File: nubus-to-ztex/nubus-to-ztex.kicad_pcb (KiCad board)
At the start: 4 copper layers, 161.6 x 100 mm, 94 parts, among them J1 Conn_02x07_Odd_Even, J2 47219-2001, J3 Conn_01x06_Male, J4 C96ABC, J5 HDMI_A, J6 USB micro-B, J7 Conn_01x03_Male, J8 Conn_01x02, J9 Conn_02x06_Odd_Even, U1 74LVT125, U10 SN65220, U11 TPS2051C, U12 SN74CB3T1G125DBVR, U13 SN74CB3T3125PWR, U14 SN74CB3T3245PWR, U2 74LVT125, U3 74LVT125, U4 SN74CB3T3125PWR, U5 74LVT245BPW,118, U6 74LVT245BPW,118, U7 74LVT245BPW,118, U8 74LVT245BPW,118, U9 TPD12S016PWR

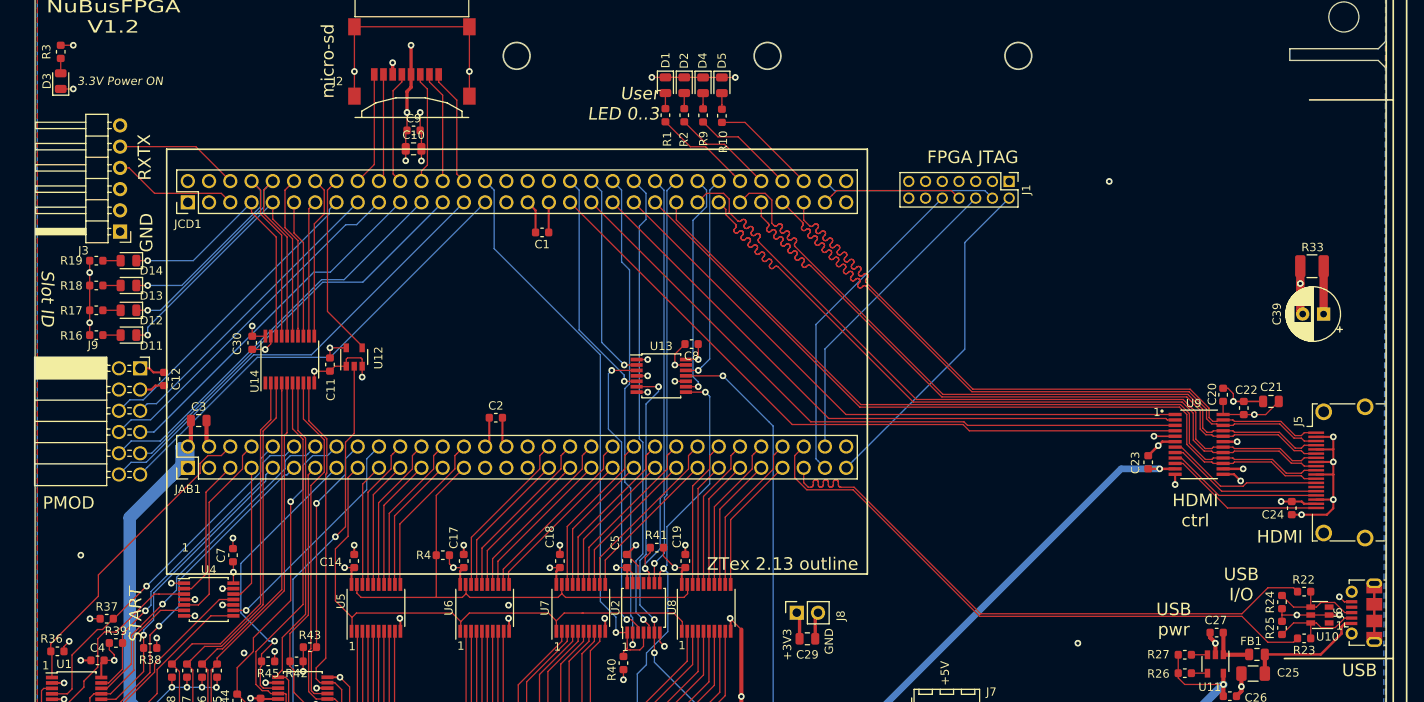
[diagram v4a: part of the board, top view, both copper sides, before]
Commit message: reinstate some useful debug LEDs
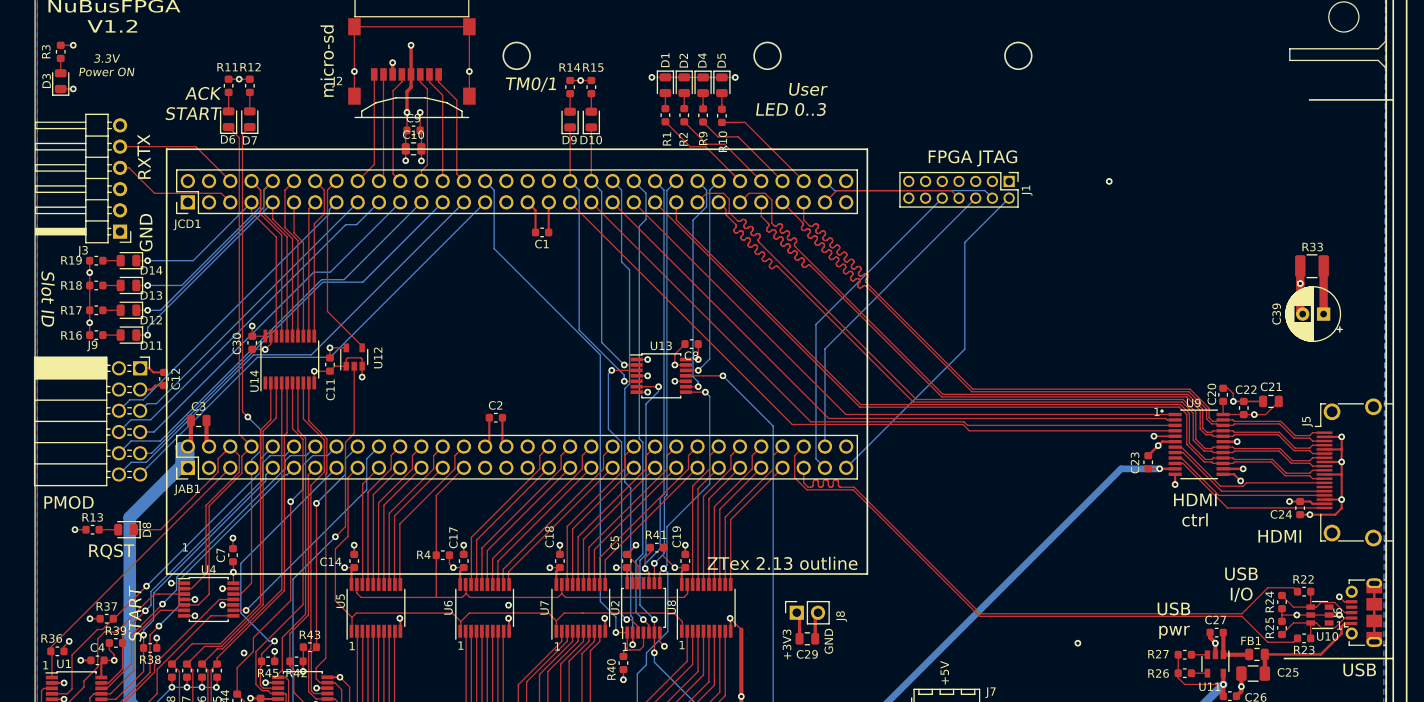
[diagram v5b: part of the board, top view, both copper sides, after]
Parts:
- added D10: YELLOW, LED_SMD:LED_0805_2012Metric, F.Cu at (178.3, 20.1)
- added D6: YELLOW, LED_SMD:LED_0805_2012Metric, F.Cu at (134.9, 20.1)
- added D7: YELLOW, LED_SMD:LED_0805_2012Metric, F.Cu at (137.4, 20.1)
- added D8: YELLOW, LED_SMD:LED_0805_2012Metric, F.Cu at (122.6, 69.2)
- added D9: YELLOW, LED_SMD:LED_0805_2012Metric, F.Cu at (175.7, 20.1)
- added R11: 549, Resistor_SMD:R_0603_1608Metric, F.Cu at (134.9, 16.1)
- added R12: 549, Resistor_SMD:R_0603_1608Metric, F.Cu at (137.4, 16.1)
- added R13: 549, Resistor_SMD:R_0603_1608Metric, F.Cu at (118.6, 69.2)
- added R14: 549, Resistor_SMD:R_0603_1608Metric, F.Cu at (175.7, 16.2)
- added R15: 549, Resistor_SMD:R_0603_1608Metric, F.Cu at (178.3, 16.2)
- moved C24 1.00 mm to (263.0, 66.6)
- moved J5 1.00 mm to (268.9, 62.3)
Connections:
- JAB1 pad 5: ~RQST_3V3 -> ~NMRQ_3V3
- JAB1 pad 6: ~NMRQ_3V3 -> ~RQST_3V3
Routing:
- net ~START_3V3: track 16.5 -> 59.0 mm, vias 0 -> 1
- net ~ACK_3V3: track 23.3 -> 62.6 mm
- net +3V3: track 737.6 -> 771.3 mm, vias 27 -> 30
- net ~RQST_3V3: track 17.3 -> 37.3 mm
- net ~TM1_3V3: track 25.1 -> 31.5 mm
- net ~TM0_3V3: track 28.1 -> 34.5 mm
- net ~NMRQ_3V3: track 37.5 -> 34.0 mm
- net Net-(D7-Pad2): track 0.00 -> 2.28 mm
- net Net-(D8-Pad2): track 0.00 -> 2.28 mm
- net Net-(D6-Pad2): track 0.00 -> 2.28 mm
- net Net-(D9-Pad2): track 0.00 -> 2.16 mm
- net Net-(D10-Pad2): track 0.00 -> 2.16 mm
- net HDMI_D2+: track 83.7 -> 84.7 mm
- net HDMI_D1-: track 87.1 -> 88.1 mm
- net HDMI_D1+: track 88.0 -> 89.0 mm
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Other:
- board text added: "ACK START"
- board text added: "RQST"
- board text added: "TM0/1"

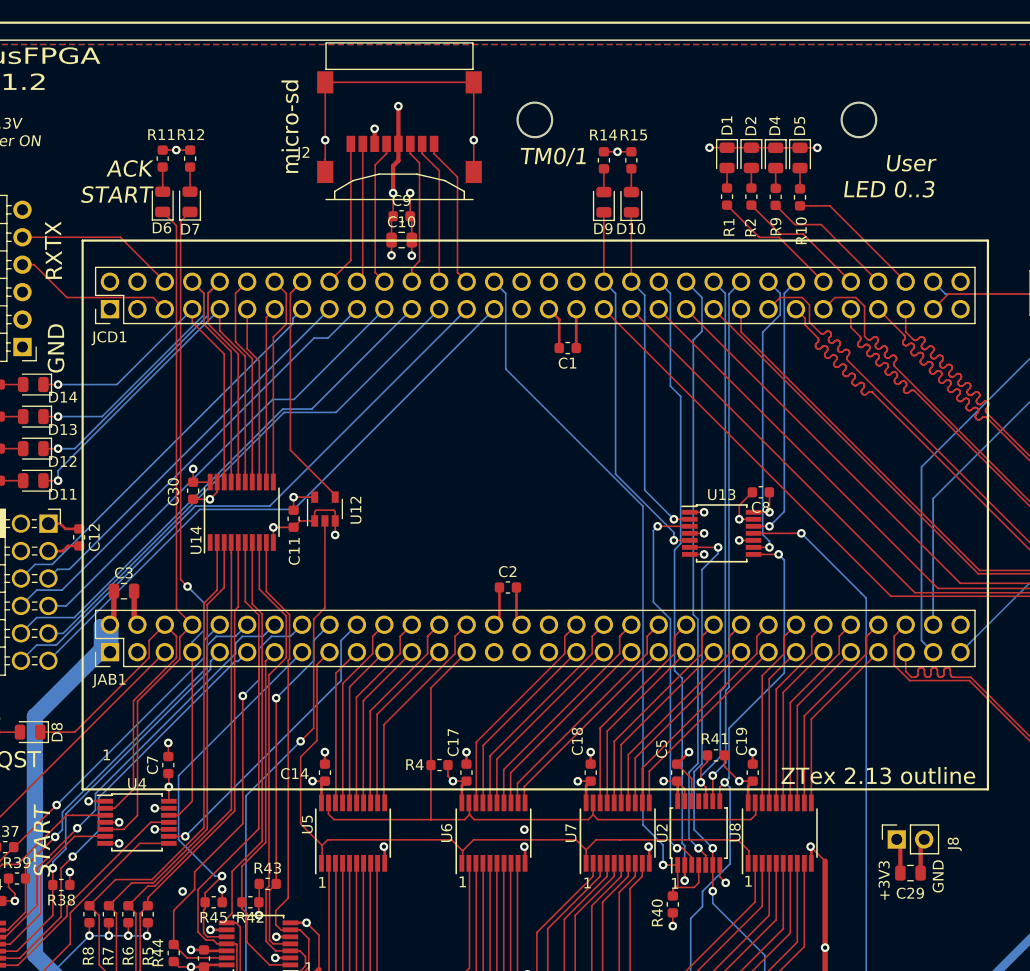
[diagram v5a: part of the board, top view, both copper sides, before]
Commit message: cut down brightness of LEDs, more 2x32 pin headers reference
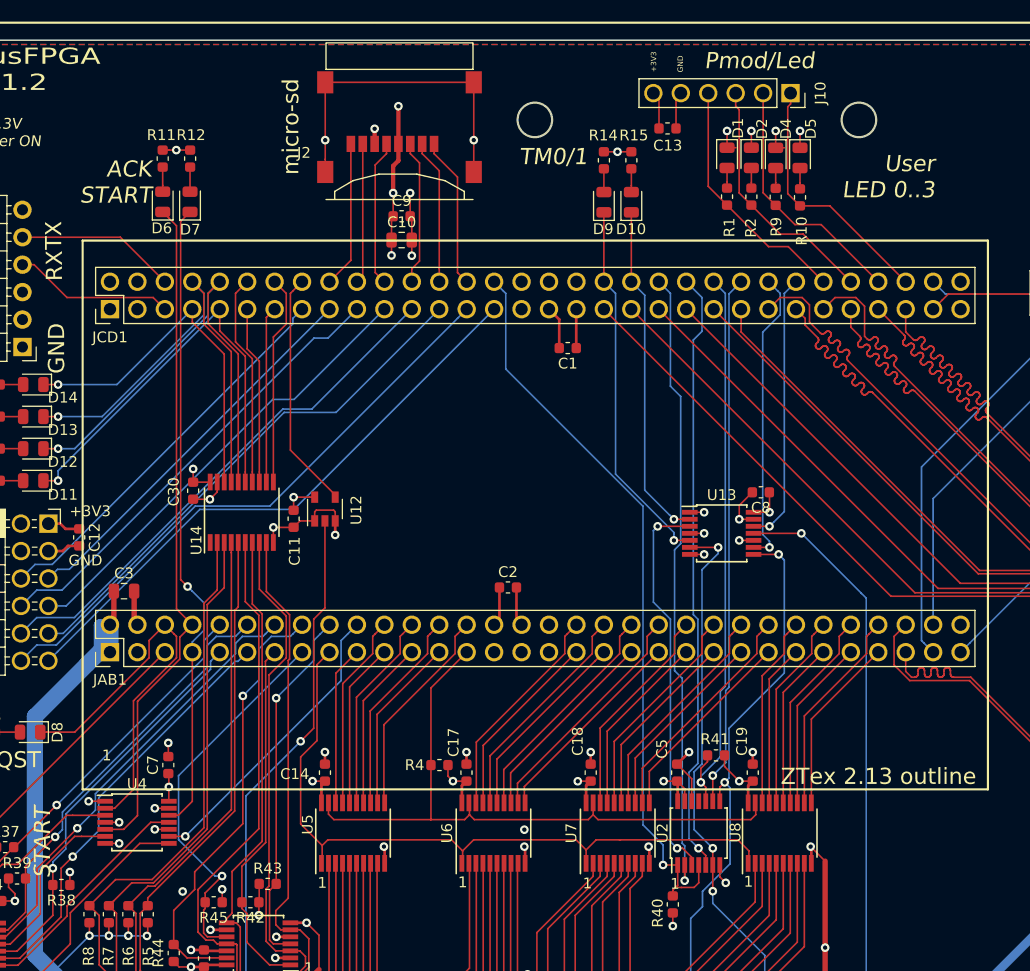
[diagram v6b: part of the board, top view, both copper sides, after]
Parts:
- removed C29: 47uF 10V+, Capacitor_SMD:C_0805_2012Metric
- removed J8: Conn_01x02, For_SeeedStudio:PinSocket_1x02_P2.54mm_Vertical_for_SeeedStudio
- added C13: 100nF, Capacitor_SMD:C_0603_1608Metric, F.Cu at (181.6, 13.3)
- added J10: Conn_01x06, For_SeeedStudio:PinSocket_1x06_P2.54mm_Vertical_For_SeeedStudio, F.Cu at (193.0, 10.0)
- R1, R10, R11, R12, R13, R14, R15, R16, R17, R18, R19, R2, R3, R9: value 549 -> 590
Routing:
- net LED0: track 11.9 -> 22.9 mm
- net LED3: track 12.7 -> 23.7 mm
- net LED1: track 12.1 -> 23.1 mm
- net LED2: track 12.4 -> 23.3 mm
- net GND: track 1283.9 -> 1277.8 mm, vias 65 -> 67
- net +3V3: track 771.3 -> 775.9 mm
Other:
- board text added: "Pmod/Led"

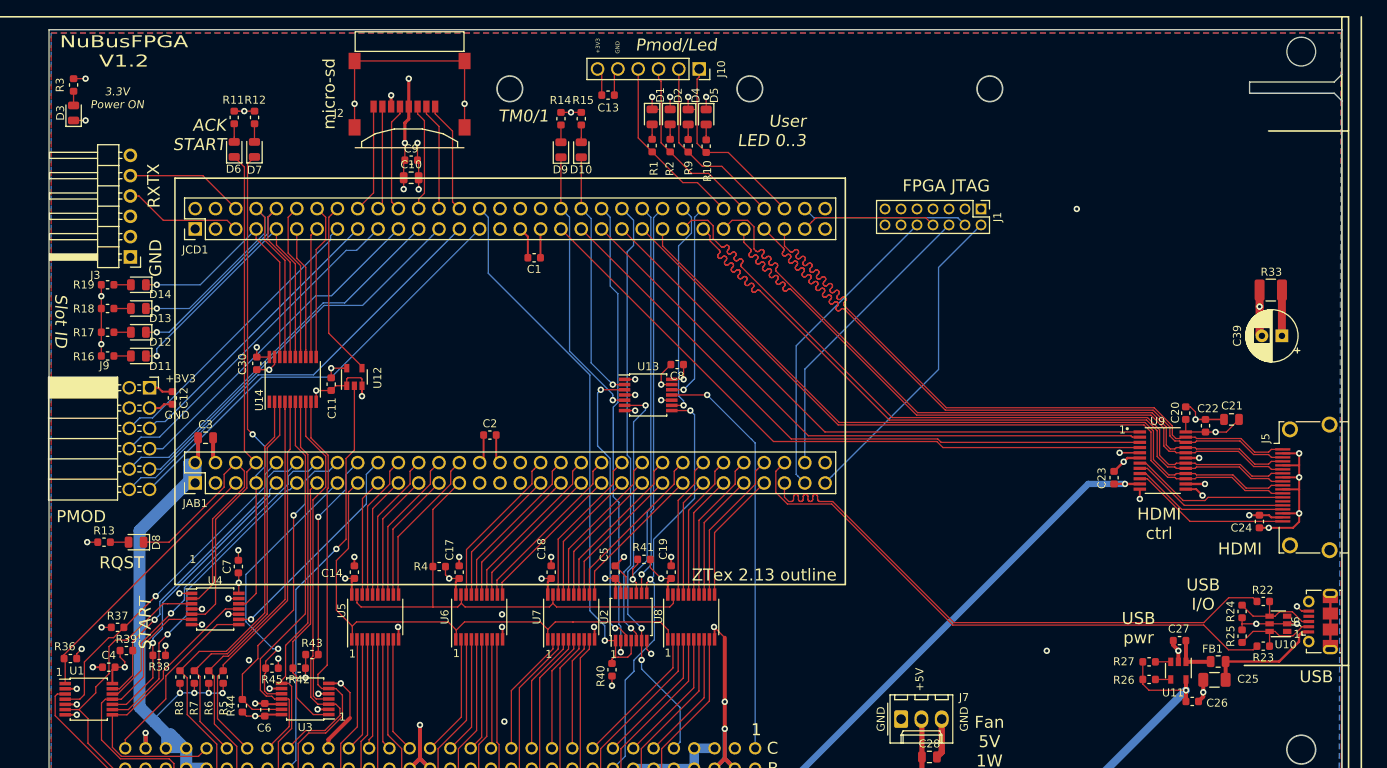
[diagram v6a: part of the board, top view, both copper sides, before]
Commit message: merge pmod & leds into an extended pmod on the outside. Also some BoM updates.
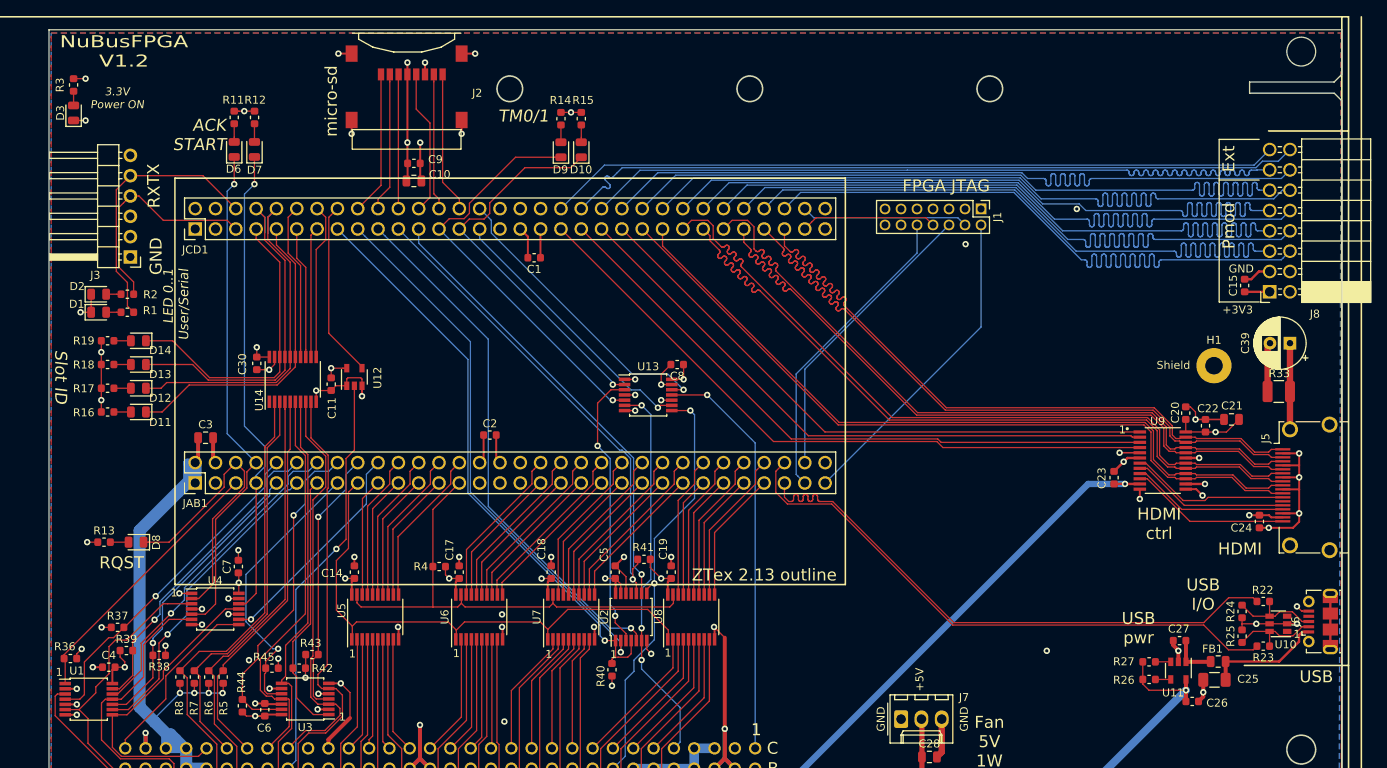
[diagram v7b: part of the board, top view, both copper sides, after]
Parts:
- removed C12, C13: 100nF, Capacitor_SMD:C_0603_1608Metric
- removed D4, D5: RED, LED_SMD:LED_0805_2012Metric
- removed J10: Conn_01x06, For_SeeedStudio:PinSocket_1x06_P2.54mm_Vertical_For_SeeedStudio
- removed J9: Conn_02x06_Odd_Even, For_SeeedStudio:PinSocket_2x06_P2.54mm_Horizontal_For_SeeedStudio
- removed R10, R9: 590, Resistor_SMD:R_0603_1608Metric
- added C15: 100nF, Capacitor_SMD:C_0603_1608Metric, F.Cu at (261.2, 37.1)
- added H1: MountingHole_Pad, MountingHole:MountingHole_2.2mm_M2_Pad, F.Cu at (257.4, 47.1)
- added J8: Conn_02x08_Odd_Even, For_SeeedStudio:PinSocket_2x08_P2.54mm_Horizontal_ForSeeedStudio, F.Cu at (264.3, 37.9)
- C10: value 47uF -> 47uF 10V+
- C25: value 150uF -> 150uF (could be >= 100 uF or even less, probably)
- moved D2 74.8 mm to (117.9, 38.2), turned to 0 degrees
- moved D1 73.4 mm to (117.9, 40.4), turned to 0 degrees
- moved R2 70.3 mm to (121.5, 38.2), turned to 180 degrees
- moved R1 68.8 mm to (121.5, 40.4), turned to 180 degrees
- moved R33 12.7 mm to (265.4, 50.3)
- moved D11 7.00 mm to (122.9, 52.9)
- moved D12 7.00 mm to (122.9, 49.9)
- moved D13 7.00 mm to (122.9, 46.9)
- moved D14 7.00 mm to (122.9, 44.0)
- moved R16 7.00 mm to (119.1, 52.9)
- moved R17 7.00 mm to (119.1, 49.9)
- moved R18 7.00 mm to (119.1, 46.9)
- moved R19 7.00 mm to (119.1, 44.0)
- moved C39 1.37 mm to (266.9, 44.3)
- moved C9 0.52 mm to (157.3, 21.8)
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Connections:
- net HDMI_5V renamed /hdmi/HDMI_5V
- J3 pad 4: /B2B/RX -> LED1
- J3 pad 5: /B2B/TX -> LED0
- JCD1 pad 15: PMOD-6 -> TMx_oe_n
- JCD1 pad 17: PMOD-5 -> TM1_n_o
- JCD1 pad 18: SD_D1 -> SD_D2
- JCD1 pad 19: PMOD-8 -> TM0_n_o
- JCD1 pad 20: SD_D0 -> SD_D3
- JCD1 pad 21: PMOD-7 -> TM2_oe_n
- JCD1 pad 22: SD_CLK -> SD_CMD
- JCD1 pad 23: PMOD-10 -> TM2_o_n
- JCD1 pad 24: SD_CMD -> SD_CLK
- JCD1 pad 25: PMOD-9 -> ~TM0_3V3
- JCD1 pad 26: SD_D3 -> SD_D0
- JCD1 pad 27: PMOD-12 -> ~TM1_3V3
- JCD1 pad 28: SD_D2 -> SD_D1
- JCD1 pad 29: PMOD-11 -> ~TM2_3V3
- JCD1 pad 30: TMx_oe_n -> ~RESET_3V3
- JCD1 pad 38: ~TM0_3V3 -> PMOD-15
- JCD1 pad 40: ~TM1_3V3 -> PMOD-16
- JCD1 pad 42: TM1_n_o -> PMOD-13
- JCD1 pad 44: TM0_n_o -> PMOD-14
- JCD1 pad 46: TM2_oe_n -> PMOD-11
- JCD1 pad 48: TM2_o_n -> PMOD-12
- JCD1 pad 5: /B2B/RX -> LED1
- JCD1 pad 50: ~TM2_3V3 -> PMOD-9
- JCD1 pad 52: ~RESET_3V3 -> PMOD-10
- JCD1 pad 54: LED0 -> PMOD-7
- JCD1 pad 56: LED1 -> PMOD-8
- JCD1 pad 58: LED2 -> PMOD-5
- JCD1 pad 6: /B2B/TX -> LED0
- JCD1 pad 60: LED3 -> PMOD-6
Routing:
- net PMOD-14: track 0.00 -> 97.5 mm
- net PMOD-13: track 0.00 -> 96.4 mm
- net PMOD-16: track 0.00 -> 93.6 mm
- net PMOD-15: track 0.00 -> 91.6 mm
- net +3V3: track 775.9 -> 720.3 mm, vias 30 -> 29
- net PMOD-5: track 36.3 -> 90.9 mm
- net PMOD-6: track 36.6 -> 89.0 mm
- net PMOD-7: track 42.5 -> 93.9 mm
- net PMOD-8: track 42.5 -> 92.8 mm
- net PMOD-9: track 48.6 -> 97.0 mm
- net PMOD-10: track 48.6 -> 95.2 mm
- net PMOD-11: track 54.7 -> 99.6 mm
- net PMOD-12: track 54.7 -> 98.2 mm
- net LED3: track 23.7 -> 0.00 mm
- net LED2: track 23.3 -> 0.00 mm
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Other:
- net class Shielding added: clearance 0.2, trace_width 0.1524, via_dia 0.8, via_drill 0.4
- board text added: "Ext"
- board text added: "LED 0..1 User/Serial"
- board text added: "Pmod"
- board text added: "Shield"
- board text removed: "PMOD"
- board text removed: "Pmod/Led"
- board text removed: "START"
- board text removed: "User LED 0..3"
